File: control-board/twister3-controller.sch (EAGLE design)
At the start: 47 parts, among them IC2 TMC2130-LA, U1 MAX6816, U2 LCD-16X2SILK, U3 IS31FL3193, U4 MIC4680-5.0YM-TR

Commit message: Pretty much done with r1.0 of control board
- Stacking PCB design
- Top PCB is a panel that fits into a plastic enclosure
- Bottom holds electronics (Teensy 3.2, LCD, motor driver, encoder, etc)
- 0.1" headers hold the two boards together
- I'm trying to use hacked GND press clips to clip the LCD PCB to the
panel board instead of screws/standoffs. The goal is the two PCBs should
snap together without screws.
- I ordered the DK parts to check fits etc. I will then make final
changes and send out PCB.
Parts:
- removed CFG1, CFG2: JUMPER3-0201, we-rcl:JUMPER3-0201
- removed JP10, JP8, JP9: (no value), pinhead:PINHD-1X1
- removed R20: 20k, we-rcl:POT-EVM3R
- removed SPI1: JUMPER2-0402-NC, we-rcl:JUMPER2-0402-NC
- removed U$1: TEENSY_3.1_ALL_PINS_AND_PADS, jonnew:TEENSY_3.1_ALL_PINS_AND_PADS
- added J10, J12, J8, J9: (no value), jonnew:PINHD-1X4
- added J11, J3, J4, J5, J6: (no value), jonnew:PINHD-1X4_SMD-0.1"
- added J2: OSTVN04A150, jonnew:PINHD-1X4
- added J7: BARREL-JACK_PJ-063BH, jonnew:BARREL-JACK_PJ-063BH
- added R10: 20k, jonnew:TRIM_US-SM-42/43W
- added R12: 4.7k, jonnew:R_0805
- added R14, R15: 4.7k, cyclops:R_0603
- added R16: 100k, jonnew:R_0805
- added S2: 800AWSP9M2QE, jonnew:SPST_TACT2_800AW
- added TP1: RESET, jonnew:TP_1MM
- added TP2, TP3, TP4: S7121-42R, jonnew:TP_S7121-42R
- added U10: Teensy 3.2, jonnew:TEENSY_3.1_CYCLOPS
- C12: device rcl:C-EUC0603 -> jonnew:C_0603
- C13, C16, C17: device we-rcl:CAPACITOR-0402 -> jonnew:C_0402
- C14: value 470n/10V -> 470nF/10V; device we-rcl:CAPACITOR-0402 -> jonnew:C_0402
- C15: value 4u7/10V -> 47uF/10V; device we-rcl:CAPACITOR-0402 -> jonnew:C_0402
- C18: value 100n/50V -> 100nF/50V; device we-rcl:CAPACITOR-0402 -> jonnew:C_0402
- C19: value 22n/50V -> 22nF/50V; device we-rcl:CAPACITOR-0402 -> jonnew:C_0402
- J1: device jonnew:PINHD-1X4_SCREW-0.1" -> jonnew:PINHD-1X4
- R18, R19: value R0805/0R11 -> 0.11; device rcl:R-EU_M0805 -> jonnew:R_0805
- R2: value (none) -> 20k
- R22: device we-rcl:RESISTOR-0402 -> jonnew:R_0402
- R23: value 2R2 -> 2.2; device we-rcl:RESISTOR-0402 -> jonnew:R_0402
- S1: value (none) -> EC12P
- U2: value LCD-16X2SILK -> GDM1602K
- U4: device jonnew:MIC4680 -> jonnew:MIC4680_SOIC
- renumbered IC2 to U11
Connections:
- net +5V renamed +5VOUT
- net N$5 renamed SW
- removed net !SHDN: U3.!SHDN
- removed net CFG-0: JP6.4, U11.SDO_NAO_CFG0
- removed net CFG-1: JP6.7, U11.SDI_NAI_CFG1
- removed net CFG-2: JP6.6, U11.SCK_CFG2
- removed net CFG-3: JP6.5, U11.CSN_CFG3
- removed net MISO: U$1.12/MISO
- removed net MOSI: U$1.11/MOSI
- removed net N$12: U$1.0/RX1/T, U2.RS
- removed net N$13: U$1.1/TX1/T, U2.R/W
- removed net N$14: U$1.2, U2.E
- removed net N$15: U$1.3/CAN-TX/PWM, U2.DB0
- removed net N$16: U$1.4/CAN-RX-PWM, U2.DB1
- removed net N$17: U$1.5/PWM, U2.DB2
- removed net N$18: U$1.6/PWM, U2.DB3
- removed net N$19: U$1.7/RX3, U2.DB4
- removed net N$20: U$1.8/TX3, U2.DB5
- removed net N$21: U$1.9/RX2/PWM, U2.DB6
- removed net N$22: U$1.10/TX2/PWM, U2.DB7
- removed net N$30: SPI1.2, U11.SPI_MODE
- removed net SCLK: U$1.13/SCK/LED
- removed net VIO: C13.2, CFG1.3, CFG2.3, JP7.7, U11.VCC_IO
- new net !IS31_SHDN: R16.1, U10.33/T, U3.!SHDN
- new net CFG-0/MISO: JP6.4, U10.12/MISO, U11.SDO_NAO_CFG0
- new net CFG-1/MOSI: JP6.7, U10.11/MOSI, U11.SDI_NAI_CFG1
- new net CFG-2/SCLK: JP6.6, U10.13/SCK/LED, U11.SCK_CFG2
- new net CFG-3/!TMC_CS: JP6.5, U10.31/A20, U11.CSN_CFG3
- new net DB0: U10.3/CAN-TX/PWM, U2.DB0
- new net DB1: U10.4/CAN-RX-PWM, U2.DB1
- new net DB2: U10.5/PWM, U2.DB2
- new net DB3: U10.6/PWM, U2.DB3
- new net DB4: U10.7/RX3, U2.DB4
- new net DB5: U10.8/TX3, U2.DB5
- new net DB6: U10.9/RX2/PWM, U2.DB6
- new net DB7: U10.10/TX2/PWM, U2.DB7
- new net E: U10.2, U2.E
- new net MECH1: J11.1, J11.2, J11.3, J11.4
- new net MECH2: J6.1, J6.2, J6.3, J6.4
- new net MECH3: J4.1, J4.2, J4.3, J4.4, TP2.TP
- new net MECH4: J5.1, J5.2, J5.3, J5.4, TP3.TP, TP4.TP
- new net N$23: S2.P, TP1.TP
- new net N$6: J2.1, J3.4
- new net N$7: J2.2, J3.3
- new net N$8: J2.3, J3.2
- new net N$9: J2.4, J3.1
- new net RS: U10.0/RX1/T, U2.RS
- new net RW: U10.1/TX1/T, U2.R/W
- new net SD_MODE: U10.16/A2/T, U11.SD_MODE
- new net SPI_MODE: U10.15/A1/T, U11.SPI_MODE
- net +24V0: now also J7.IN
- net +3V3: now also C13.2, JP7.7, U10.3.3V, U11.VCC_IO; no longer R1.2, R2.A, R3.1, R6.2, R7.1, U$1.3.3V, U2.A, U2.VDD
- net +5V0: now also R1.2, R12.2, R14.2, R15.2, R2.A, R3.1, R6.2, R7.1, U10.VIN, U2.A, U2.VDD; no longer U$1.VIN
- net BUTT: now also U10.21/A7/PWM; no longer U$1.16/A2/T
- net CFG-6: now also U10.26/A15
- net CFG4: now also U10.14/A0; no longer CFG1.2
- net CFG5: now also U10.30/A19/SDA1; no longer CFG2.2
- net DIAG0: now also R15.1, U10.29/A18/SCL1; no longer JP8.1
- net DIAG1: now also R14.1, U10.28/A17; no longer JP9.1
- net DIR: now also U10.17/A3/T; no longer U$1.21/A7/PWM
- net ENC_A: now also U10.22/A8/T/PWM; no longer U$1.14/A0
- net ENC_B: now also U10.23/A9/T/PWM; no longer U$1.15/A1/T
- net GND: now also J7.OUT, R10.E, R16.2, S2.S, U10.GND; no longer CFG1.1, CFG2.1, R20.E, SPI1.1, U$1.GND
- net IREF: now also R10.W; no longer JP10.1, R20.S
- net SCL: now also U10.19/A5/T/SCL0; no longer U$1.19/A5/T/SCL0
- net SDA: now also U10.18/A4/T/SDA0; no longer U$1.18/A4/T/SDA0
- net STEP: now also U10.32/T/PWM; no longer U$1.20/A6/PWM
- net VREF2: now also R10.A; no longer R20.A
- net V_BM: now also R12.1
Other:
- note added: "Clips hold up LCD"
- note added: "Mechanical connections between panel and board."
- note added: "Motor connection to screw terminal"
- note added: "Teensy reset (jumper wire to reset pad on Teensy)"
- moved on the sheet: C5, C6, JP7, R2, R3, R7, U2

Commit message: Complete rev 1.0 of control board
- Off to fab
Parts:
- U2: device SparkFun-Displays:LCD-16X2SILK -> jonnew:LCD-16X2SILK
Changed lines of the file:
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@@
 <grid distance="0.1" unitdist="inch" unit="inch" style="lines" multiple="1" display="no" altdistance="0.01" altunitdist="inch" altunit="inch"/>
 <layers>
-<layer number="1" name="Top" color="4" fill="1" visible="yes" active="no"/>
-<layer number="2" name="Route2" color="1" fill="3" visible="yes" active="no"/>
-<layer number="3" name="Route3" color="4" fill="3" visible="yes" active="no"/>
-<layer number="4" name="Route4" color="1" fill="4" visible="yes" active="no"/>
-<layer number="5" name="Route5" color="4" fill="4" visible="yes" active="no"/>
-<layer number="6" name="Route6" color="1" fill="8" visible="yes" active="no"/>
-<layer number="7" name="Route7" color="4" fill="8" visible="yes" active="no"/>
-<layer number="8" name="Route8" color="1" fill="2" visible="yes" active="no"/>
-<layer number="9" name="Route9" color="4" fill="2" visible="yes" active="no"/>
-<layer number="10" name="Route10" color="1" fill="7" visible="yes" active="no"/>
-<layer number="11" name="Route11" color="4" fill="7" visible="yes" active="no"/>
-<layer number="12" name="Route12" color="1" fill="5" visible="yes" active="no"/>
-<layer number="13" name="Route13" color="4" fill="5" visible="yes" active="no"/>
-<layer number="14" name="Route14" color="1" fill="6" visible="yes" active="no"/>
-<layer number="15" name="Route15" color="4" fill="6" visible="yes" active="no"/>
-<layer number="16" name="Bottom" color="1" fill="1" visible="yes" active="no"/>
-<layer number="17" name="Pads" color="2" fill="1" visible="yes" active="no"/>
-<layer number="18" name="Vias" color="2" fill="1" visible="yes" active="no"/>
-<layer number="19" name="Unrouted" color="6" fill="1" visible="yes" active="no"/>
-<layer number="20" name="Dimension" color="24" fill="1" visible="yes" active="no"/>
-<layer number="21" name="tPlace" color="7" fill="1" visible="yes" active="no"/>
-<layer number="22" name="bPlace" color="7" fill="1" visible="yes" active="no"/>
-<layer number="23" name="tOrigins" color="15" fill="1" visible="yes" active="no"/>
-<layer number="24" name="bOrigins" color="15" fill="1" visible="yes" active="no"/>
-<layer number="25" name="tNames" color="7" fill="1" visible="yes" active="no"/>
-<layer number="26" name="bNames" color="7" fill="1" visible="yes" active="no"/>
-<layer number="27" name="tValues" color="7" fill="1" visible="yes" active="no"/>
-<layer number="28" name="bValues" color="7" fill="1" visible="yes" active="no"/>
+<layer number="1" name="Top" color="4" fill="1" visible="no" active="no"/>
+<layer number="2" name="Route2" color="1" fill="3" visible="no" active="no"/>
+<layer number="3" name="Route3" color="4" fill="3" visible="no" active="no"/>
+<layer number="4" name="Route4" color="1" fill="4" visible="no" active="no"/>
+<layer number="5" name="Route5" color="4" fill="4" visible="no" active="no"/>
+<layer number="6" name="Route6" color="1" fill="8" visible="no" active="no"/>
+<layer number="7" name="Route7" color="4" fill="8" visible="no" active="no"/>
+<layer number="8" name="Route8" color="1" fill="2" visible="no" active="no"/>
+<layer number="9" name="Route9" color="4" fill="2" visible="no" active="no"/>
+<layer number="10" name="Route10" color="1" fill="7" visible="no" active="no"/>
+<layer number="11" name="Route11" color="4" fill="7" visible="no" active="no"/>
+<layer number="12" name="Route12" color="1" fill="5" visible="no" active="no"/>
+<layer number="13" name="Route13" color="4" fill="5" visible="no" active="no"/>
+<layer number="14" name="Route14" color="1" fill="6" visible="no" active="no"/>
+<layer number="15" name="Route15" color="4" fill="6" visible="no" active="no"/>
+<layer number="16" name="Bottom" color="1" fill="1" visible="no" active="no"/>
+<layer number="17" name="Pads" color="2" fill="1" visible="no" active="no"/>
+<layer number="18" name="Vias" color="2" fill="1" visible="no" active="no"/>
+<layer number="19" name="Unrouted" color="6" fill="1" visible="no" active="no"/>
+<layer number="20" name="Dimension" color="24" fill="1" visible="no" active="no"/>
+<layer number="21" name="tPlace" color="7" fill="1" visible="no" active="no"/>
+<layer number="22" name="bPlace" color="7" fill="1" visible="no" active="no"/>
+<layer number="23" name="tOrigins" color="15" fill="1" visible="no" active="no"/>
+<layer number="24" name="bOrigins" color="15" fill="1" visible="no" active="no"/>
+<layer number="25" name="tNames" color="7" fill="1" visible="no" active="no"/>
+<layer number="26" name="bNames" color="7" fill="1" visible="no" active="no"/>
+<layer number="27" name="tValues" color="7" fill="1" visible="no" active="no"/>
+<layer number="28" name="bValues" color="7" fill="1" visible="no" active="no"/>
 <layer number="29" name="tStop" color="7" fill="3" visible="no" active="no"/>
 <layer number="30" name="bStop" color="7" fill="6" visible="no" active="no"/>
@@
 <layer number="35" name="tGlue" color="7" fill="4" visible="no" active="no"/>
 <layer number="36" name="bGlue" color="7" fill="5" visible="no" active="no"/>
-<layer number="37" name="tTest" color="7" fill="1" visible="yes" active="no"/>
-<layer number="38" name="bTest" color="7" fill="1" visible="yes" active="no"/>
+<layer number="37" name="tTest" color="7" fill="1" visible="no" active="no"/>
+<layer number="38" name="bTest" color="7" fill="1" visible="no" active="no"/>
 <layer number="39" name="tKeepout" color="4" fill="11" visible="no" active="no"/>
 <layer number="40" name="bKeepout" color="1" fill="11" visible="no" active="no"/>
@@
 <layer number="44" name="Drills" color="7" fill="1" visible="no" active="no"/>
 <layer number="45" name="Holes" color="7" fill="1" visible="no" active="no"/>
-<layer number="46" name="Milling" color="3" fill="1" visible="yes" active="no"/>
-<layer number="47" name="Measures" color="7" fill="1" visible="yes" active="no"/>
-<layer number="48" name="Document" color="7" fill="1" visible="yes" active="no"/>
-<layer number="49" name="Reference" color="7" fill="1" visible="yes" active="no"/>
-<layer number="50" name="dxf" color="7" fill="1" visible="yes" active="no"/>
-<layer number="51" name="tDocu" color="7" fill="1" visible="yes" active="no"/>
-<layer number="52" name="bDocu" color="7" fill="1" visible="yes" active="no"/>
-<layer number="53" name="tGND_GNDA" color="7" fill="9" visible="yes" active="no"/>
-<layer number="54" name="bGND_GNDA" color="1" fill="9" visible="yes" active="no"/>
-<layer number="56" name="wert" color="7" fill="1" visible="yes" active="no"/>
-<layer number="57" name="tCAD" color="7" fill="1" visible="yes" active="no"/>
-<layer number="59" name="tCarbon" color="7" fill="1" visible="yes" active="no"/>
-<layer number="60" name="bCarbon" color="7" fill="1" visible="yes" active="no"/>
+<layer number="46" name="Milling" color="3" fill="1" visible="no" active="no"/>
+<layer number="47" name="Measures" color="7" fill="1" visible="no" active="no"/>
+<layer number="48" name="Document" color="7" fill="1" visible="no" active="no"/>
+<layer number="49" name="Reference" color="7" fill="1" visible="no" active="no"/>
+<layer number="50" name="dxf" color="7" fill="1" visible="no" active="no"/>
+<layer number="51" name="tDocu" color="7" fill="1" visible="no" active="no"/>
+<layer number="52" name="bDocu" color="7" fill="1" visible="no" active="no"/>
+<layer number="53" name="tGND_GNDA" color="7" fill="9" visible="no" active="no"/>
+<layer number="54" name="bGND_GNDA" color="1" fill="9" visible="no" active="no"/>
+<layer number="56" name="wert" color="7" fill="1" visible="no" active="no"/>
+<layer number="57" name="tCAD" color="7" fill="1" visible="no" active="no"/>
+<layer number="59" name="tCarbon" color="7" fill="1" visible="no" active="no"/>
+<layer number="60" name="bCarbon" color="7" fill="1" visible="no" active="no"/>
 <layer number="90" name="Modules" color="5" fill="1" visible="yes" active="yes"/>
 <layer number="91" name="Nets" color="2" fill="1" visible="yes" active="yes"/>
@@
 <part name="R1" library="jonnew" deviceset="R" device="_0805" value="10k"/>
 <part name="S1" library="SparkFun-Switches" deviceset="ENCODER-RGB-SWITCH" device="" value="EC12P"/>
-<part name="U2" library="SparkFun-Displays" deviceset="LCD-16X2" device="SILK" value="GDM1602K"/>
+<part name="U2" library="jonnew" deviceset="LCD-16X2" device="SILK" value="GDM1602K"/>
 <part name="R4" library="jonnew" deviceset="R" device="_0805" value="10k"/>
 <part name="C2" library="jonnew" deviceset="C" device="_0805" value="10nF"/>

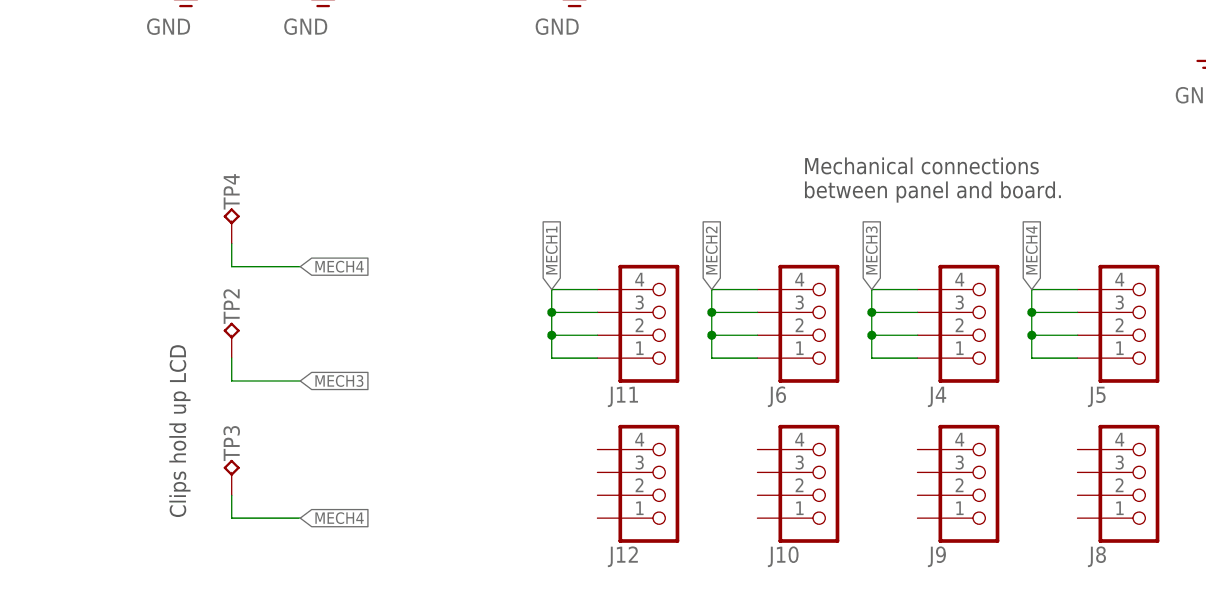
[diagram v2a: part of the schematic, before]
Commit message: Updated control board after assembly
- Removed redudant mechanical connectors
- Added positions for SMD nuts on bottom of panel board
- Replace most 0805 components with 0603
- Other minor changes
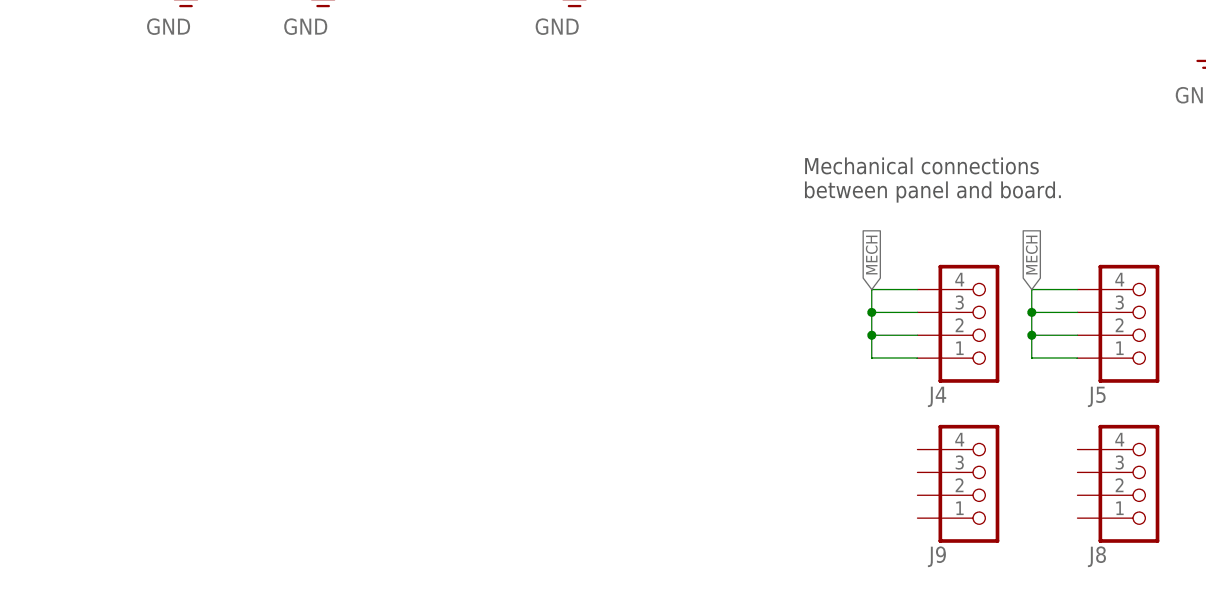
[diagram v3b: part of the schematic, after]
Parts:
- removed J10, J12: (no value), jonnew:PINHD-1X4
- removed J11, J6: (no value), jonnew:PINHD-1X4_SMD-0.1"
- removed TP2, TP3, TP4: S7121-42R, jonnew:TP_S7121-42R
- C1, C2, C3, C4, C5, C6: device jonnew:C_0805 -> jonnew:C_0603
- R1, R12, R16, R3, R4, R5, R6, R7: device jonnew:R_0805 -> jonnew:R_0603
- R10, R2: device jonnew:TRIM_US-SM-42/43W -> jonnew:TRIM_US-SM-42/43X
- R22: device jonnew:R_0402 -> jonnew:R_0603
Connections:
- removed net MECH1: J11.1, J11.2, J11.3, J11.4
- removed net MECH2: J6.1, J6.2, J6.3, J6.4
- removed net MECH3: J4.1, J4.2, J4.3, J4.4, TP2.TP
- removed net MECH4: J5.1, J5.2, J5.3, J5.4, TP3.TP, TP4.TP
- new net MECH: J4.1, J4.2, J4.3, J4.4, J5.1, J5.2, J5.3, J5.4
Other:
- note removed: "Clips hold up LCD"
